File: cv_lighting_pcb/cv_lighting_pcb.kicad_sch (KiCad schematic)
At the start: 10 parts

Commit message: cv lighting schematic
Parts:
- added +32V: ~, symbol cv_lighting_symbols:+32V
- added D10, D11, D12, D13, D14, D15, D17, D9: D_TVS, symbol Device:D_Zener
- added Q1: 2N3906, Package_TO_SOT_THT:TO-92_Inline, symbol Transistor_BJT:2N3906
- added R2: 5K, symbol Device:R
- added R3: 1K, symbol Device:R
- added RV1: R_Potentiometer_US, symbol Device:R_Potentiometer_US
- added U3: VO615A-9, symbol Isolator:VO615A-9
- R1: value R -> 5K
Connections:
- net +36V is gone; now on net GND: U1. (Vin)
- net at D1.1 (K), D2.2 (A): now also D17.2 (A), D9.1 (K)
- net at D1.2 (A), U1. (Vin): now also D17.1 (K)
- net at D4.1 (K), D5.2 (A): now also D11.2 (A), D12.1 (K)
- net at D3.1 (K), D4.2 (A): now also D10.2 (A), D11.1 (K)
- net at D8.1 (K), U1. (Vin): now also D15.2 (A), U3.3
- net at D5.1 (K), D6.2 (A): now also D12.2 (A), D13.1 (K)
- net at D2.1 (K), D3.2 (A): now also D10.1 (K), D9.2 (A)
- net at D7.1 (K), D8.2 (A): now also D14.2 (A), D15.1 (K)
- net at D6.1 (K), D7.2 (A): now also D13.2 (A), D14.1 (K)
- net at R1.1: now also U1. (Vin), Q1.1 (E), R2.2, RV1.2, RV1.3, U3.4
- net at R1.2: now also Q1.2 (B), R2.1
- new net: Q1.3 (C), RV1.1, U1. (Vin)
- new net: R3.2, U3.1
- new net +32V: +32V.1 (+32V), U1. (Vin)
- new net PWM ground: U3.2
- new net PWM input: R3.1
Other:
- moved on the sheet: D2, D3, D4, D5, D6, D7, D8

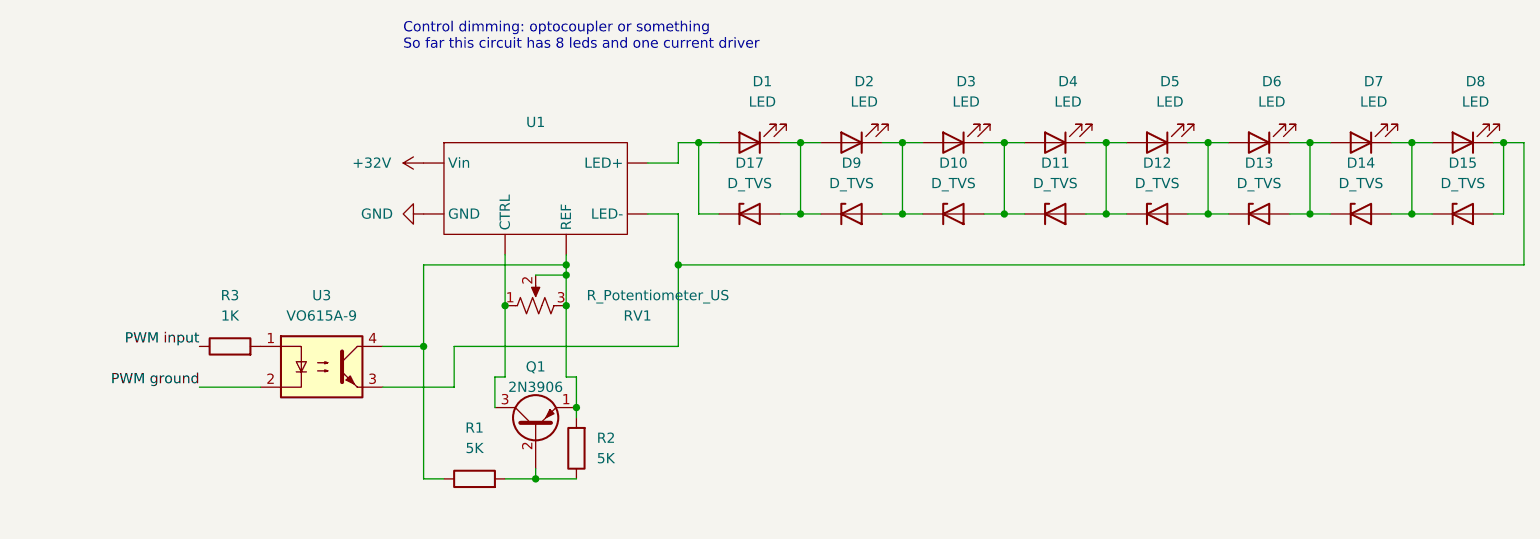
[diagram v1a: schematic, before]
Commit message: cv lighting schematic almost done, footprints all there
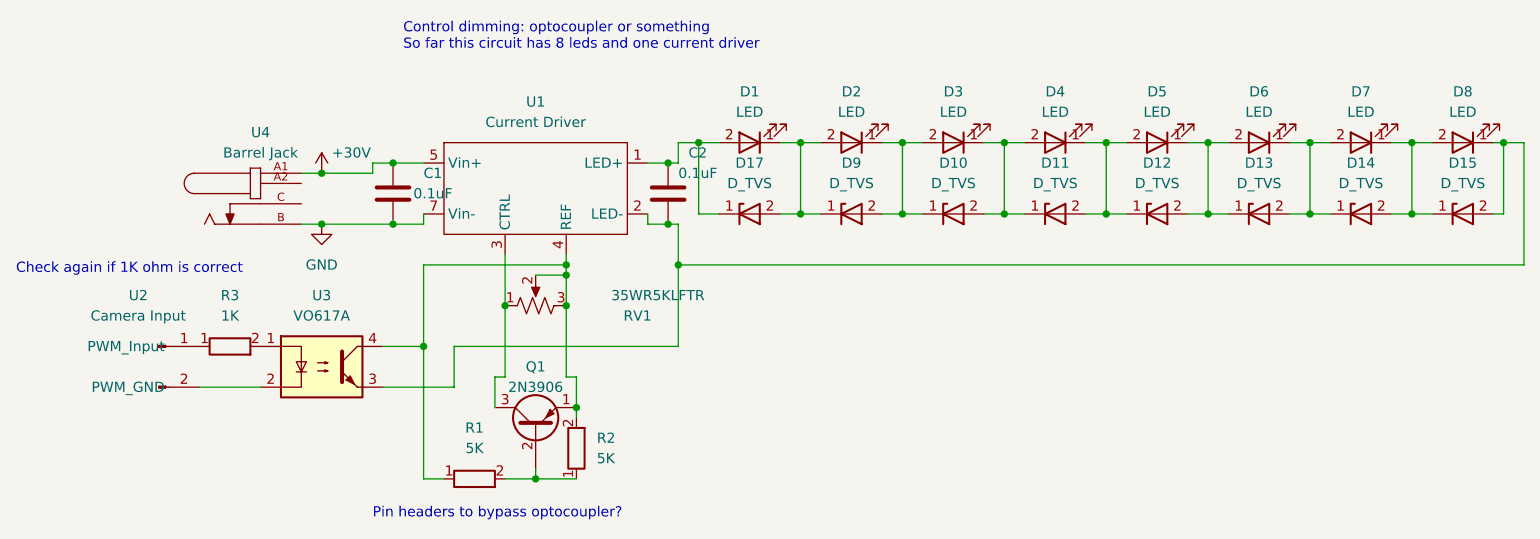
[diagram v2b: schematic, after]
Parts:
- removed +32V: ~, symbol cv_lighting_symbols:+32V
- added C1, C2: 0.1uF, Capacitor_SMD:C_0805_2012Metric_Pad1.18x1.45mm_HandSolder, symbol Device:C
- added U2: Camera Input, Connector_PinSocket_2.54mm:PinSocket_1x02_P2.54mm_Vertical_SMD_Pin1Left, symbol cv_lighting_symbols:Camera
- added U4: Barrel Jack, cv_lighting_footprints:TENSILITY_54-00164, symbol cv_lighting_symbols:Barrel_Jack
- D1, D2, D3, D4, D5, D6, D7, D8: footprint (none) -> cv_lighting_footprints:LED_SFH4715AS
- D10, D11, D12, D13, D14, D15, D17, D9: footprint (none) -> cv_lighting_footprints:D3V3M1U2S9-7
- Q1: footprint Package_TO_SOT_THT:TO-92_Inline -> cv_lighting_footprints:2N3906
- R1, R2, R3: footprint (none) -> Resistor_SMD:R_0805_2012Metric_Pad1.20x1.40mm_HandSolder
- RV1: value R_Potentiometer_US -> 35WR5KLFTR; footprint (none) -> cv_lighting_footprints:35WR5KLFTR
- U1: value ~ -> Current Driver; footprint (none) -> cv_lighting_footprints:3021_Buckpuck
- U3: value VO615A-9 -> VO617A; footprint (none) -> cv_lighting_footprints:VO617A
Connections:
- net GND: now also U1.7 (Vin-), C1.2, U4.B; no longer U1. (Vin)
- net at D1.2 (A), D17.1 (K): now also U1.1 (LED+), C2.1; no longer U1. (Vin)
- net at Q1.3 (C), RV1.1: now also U1.3 (CTRL); no longer U1. (Vin)
- net at Q1.1 (E), R1.1, R2.2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: now also U1.4 (REF); no longer U1. (Vin)
- net at D15.2 (A), D8.1 (K), U3.3: now also U1.2 (LED-), C2.2; no longer U1. (Vin)
- removed net +32V: U1. (Vin)
- net PWM ground: no longer names the net of U3.2
- net PWM ground: now also U2.2 (PWM_GND)
- net PWM input: no longer names the net of R3.1
- net PWM input: now also U2.1 (PWM_Input)
- new net +30V: C1.1, U1.5 (Vin+), U4.A1
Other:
- note added: "Check again if 1K ohm is correct"
- note added: "Pin headers to bypass optocoupler?"
